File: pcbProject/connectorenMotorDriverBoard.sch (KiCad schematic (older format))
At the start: 16 parts, among them P5 GND, P6 +5V

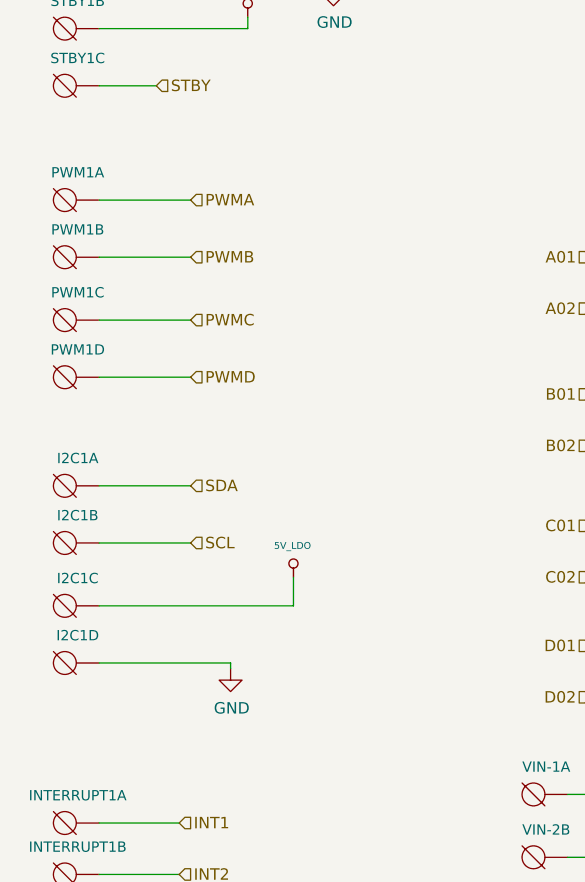
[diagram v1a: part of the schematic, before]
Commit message: TekeningAfenGecontroleerd
nu nog componenten toevoegen en routen
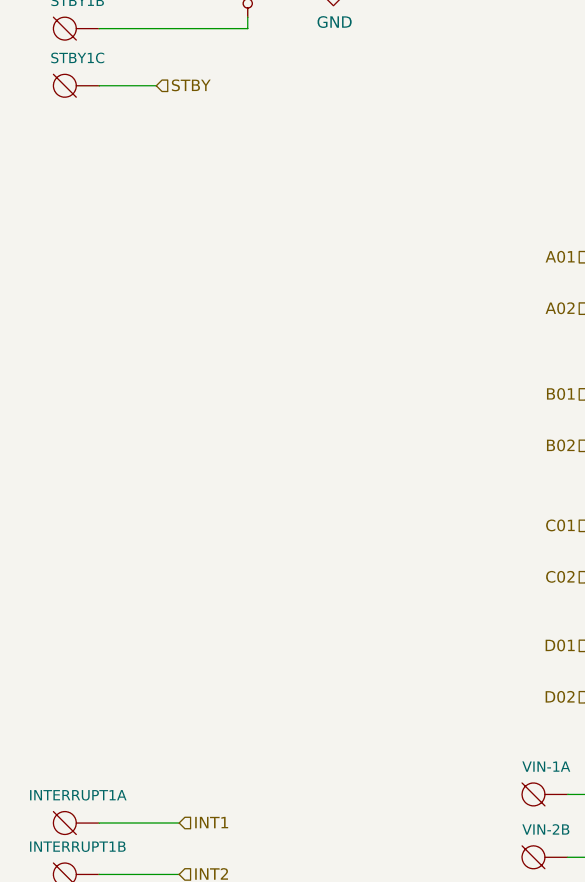
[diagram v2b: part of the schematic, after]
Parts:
- removed I2C1, PWM1: DG3XX-04-3.5, degson_DG350-3.5-04P, symbol degson:DG3XX-04-3.5
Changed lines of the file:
@@
 $Descr A4 11693 8268
 encoding utf-8
-Sheet 11 11
+Sheet 10 11
 Title ""
 Date ""
@@
 Connection ~ 4925 2125
 $Comp
-L degson:DG3XX-04-3.5 PWM1
-U 1 1 5C767F10
-P 1575 2700
-F 0 "PWM1" H 1569 2580 45  0000 C CNN
-F 1 "DG3XX-04-3.5" H 1575 2700 45  0001 L BNN
-F 2 "degson_DG350-3.5-04P" H 1605 2850 20  0001 C CNN
-F 3 "" H 1575 2700 50  0001 C CNN
-	1    1575 2700
-	-1   0    0    1
-$EndComp
-$Comp
-L degson:DG3XX-04-3.5 PWM1
-U 2 1 5C767FA5
-P 1575 2950
-F 0 "PWM1" H 1569 2830 45  0000 C CNN
-F 1 "DG3XX-04-3.5" H 1575 2950 45  0001 L BNN
-F 2 "degson_DG350-3.5-04P" H 1605 3100 20  0001 C CNN
-F 3 "" H 1575 2950 50  0001 C CNN
-	2    1575 2950
-	-1   0    0    1
-$EndComp
-$Comp
-L degson:DG3XX-04-3.5 PWM1
-U 3 1 5C76807E
-P 1575 3225
-F 0 "PWM1" H 1569 3105 45  0000 C CNN
-F 1 "DG3XX-04-3.5" H 1575 3225 45  0001 L BNN
-F 2 "degson_DG350-3.5-04P" H 1605 3375 20  0001 C CNN
-F 3 "" H 1575 3225 50  0001 C CNN
-	3    1575 3225
-	-1   0    0    1
-$EndComp
-$Comp
-L degson:DG3XX-04-3.5 PWM1
-U 4 1 5C768129
-P 1575 3475
-F 0 "PWM1" H 1569 3355 45  0000 C CNN
-F 1 "DG3XX-04-3.5" H 1575 3475 45  0001 L BNN
-F 2 "degson_DG350-3.5-04P" H 1605 3625 20  0001 C CNN
-F 3 "" H 1575 3475 50  0001 C CNN
-	4    1575 3475
-	-1   0    0    1
-$EndComp
-Text HLabel 2075 2700 2    50   Input ~ 0
-PWMA
-Text HLabel 2075 2950 2    50   Input ~ 0
-PWMB
-Text HLabel 2075 3225 2    50   Input ~ 0
-PWMC
-Text HLabel 2075 3475 2    50   Input ~ 0
-PWMD
-Wire Wire Line
-	1675 2700 2075 2700
-Wire Wire Line
-	1675 2950 2075 2950
-Wire Wire Line
-	1675 3225 2075 3225
-Wire Wire Line
-	1675 3475 2075 3475
-$Comp
-L degson:DG3XX-04-3.5 I2C1
-U 1 1 5C769E25
-P 1575 3950
-F 0 "I2C1" H 1569 3830 45  0000 C CNN
-F 1 "DG3XX-04-3.5" H 1575 3950 45  0001 L BNN
-F 2 "degson_DG350-3.5-04P" H 1605 4100 20  0001 C CNN
-F 3 "" H 1575 3950 50  0001 C CNN
-	1    1575 3950
-	-1   0    0    1
-$EndComp
-$Comp
-L degson:DG3XX-04-3.5 I2C1
-U 2 1 5C769E2C
-P 1575 4200
-F 0 "I2C1" H 1569 4080 45  0000 C CNN
-F 1 "DG3XX-04-3.5" H 1575 4200 45  0001 L BNN
-F 2 "degson_DG350-3.5-04P" H 1605 4350 20  0001 C CNN
-F 3 "" H 1575 4200 50  0001 C CNN
-	2    1575 4200
-	-1   0    0    1
-$EndComp
-$Comp
-L degson:DG3XX-04-3.5 I2C1
-U 3 1 5C769E33
-P 1575 4475
-F 0 "I2C1" H 1569 4355 45  0000 C CNN
-F 1 "DG3XX-04-3.5" H 1575 4475 45  0001 L BNN
-F 2 "degson_DG350-3.5-04P" H 1605 4625 20  0001 C CNN
-F 3 "" H 1575 4475 50  0001 C CNN
-	3    1575 4475
-	-1   0    0    1
-$EndComp
-$Comp
-L degson:DG3XX-04-3.5 I2C1
-U 4 1 5C769E3A
-P 1575 4725
-F 0 "I2C1" H 1569 4605 45  0000 C CNN
-F 1 "DG3XX-04-3.5" H 1575 4725 45  0001 L BNN
-F 2 "degson_DG350-3.5-04P" H 1605 4875 20  0001 C CNN
-F 3 "" H 1575 4725 50  0001 C CNN
-	4    1575 4725
-	-1   0    0    1
-$EndComp
-Text HLabel 2075 3950 2    50   Input ~ 0
-SDA
-Text HLabel 2075 4200 2    50   Input ~ 0
-SCL
-Wire Wire Line
-	1675 3950 2075 3950
-Wire Wire Line
-	1675 4200 2075 4200
-$Comp
-L Arduino_Uno_R3_From_Scratch:5V_LDO #PWR0122
-U 1 1 5C76B0F4
-P 2525 4350
-F 0 "#PWR0122" H 2525 4440 20  0001 C CNN
-F 1 "5V_LDO" H 2521 4488 30  0000 C CNN
-F 2 "" H 2525 4350 60  0000 C CNN
-F 3 "" H 2525 4350 60  0000 C CNN
-	1    2525 4350
-	1    0    0    -1
-$EndComp
-Wire Wire Line
-	2525 4475 2525 4350
-Wire Wire Line
-	1675 4475 2525 4475
-$Comp
-L power:GND #PWR0123
-U 1 1 5C76C27D
-P 2250 4750
-F 0 "#PWR0123" H 2250 4500 50  0001 C CNN
-F 1 "GND" H 2255 4577 50  0000 C CNN
-F 2 "" H 2250 4750 50  0001 C CNN
-F 3 "" H 2250 4750 50  0001 C CNN
-	1    2250 4750
-	1    0    0    -1
-$EndComp
-Wire Wire Line
-	2250 4725 2250 4750
-Wire Wire Line
-	1675 4725 2250 4725
-$Comp
 L degson:DG3XX-03-3.5 INTERRUPT1

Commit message: deel1routingpcb
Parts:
- removed INTERRUPT1, STBY1: DG3XX-03-3.5, degson_DG350-3.5-03P, symbol degson:DG3XX-03-3.5
- removed MA-1, MA-2, MB-1, MB-2, MC-1, MC-2, MD-1, MD-2, VIN-1, VIN-2: DG3XX-02-3.5, degson_DG350-3.5-02P, symbol degson:DG3XX-02-3.5
- added GND1: 12V, degson:degson-DG306-5.0-02P, symbol Connector:Conn_01x02_Female
- added J1: INTERRUPT, Connector_PinSocket_2.54mm:PinSocket_1x03_P2.54mm_Vertical, symbol Connector:Conn_01x03_Female
- added J2: STBY, Connector_PinSocket_2.54mm:PinSocket_1x03_P2.54mm_Vertical, symbol Connector:Conn_01x03_Female
- added MA-1A1: MA-2B, degson:degson-DG306-5.0-02P, symbol Connector:Conn_01x02_Female
- added MB-1A1: MB-2B, degson:degson-DG306-5.0-02P, symbol Connector:Conn_01x02_Female
- added MC-1A1: MC-2B, degson:degson-DG306-5.0-02P, symbol Connector:Conn_01x02_Female
- added MD-1A1: MD-2B, degson:degson-DG306-5.0-02P, symbol Connector:Conn_01x02_Female
- P5, P6: footprint (none) -> Connector_PinSocket_2.54mm:PinSocket_1x08_P2.54mm_Vertical
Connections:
- net 5V_LDO: now also J2.2 (Pin_2)
- net A01: now also MA-1A1.1 (Pin_1)
- net A02: now also MA-1A1.2 (Pin_2)
- net B01: now also MB-1A1.1 (Pin_1)
- net B02: now also MB-1A1.2 (Pin_2)
- net C01: now also MC-1A1.1 (Pin_1)
- net C02: now also MC-1A1.2 (Pin_2)
- net D01: now also MD-1A1.1 (Pin_1)
- net D02: now also MD-1A1.2 (Pin_2)
- net GND: now also GND1.1 (Pin_1), J1.1 (Pin_1), J2.1 (Pin_1)
- net INT1: now also J1.2 (Pin_2)
- net INT2: now also J1.3 (Pin_3)
- net STBY: now also J2.3 (Pin_3)
- net VM: now also GND1.2 (Pin_2)

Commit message: verslag
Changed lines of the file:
@@
 	4925 2225 4925 2125
 Connection ~ 4925 2125
-Text HLabel 3825 2950 0    50   Input ~ 0
+Text HLabel 5250 2950 0    50   Input ~ 0
 A01
-Text HLabel 3825 3175 0    50   Input ~ 0
+Text HLabel 5250 3175 0    50   Input ~ 0
 A02
 $Comp
 L power:GND #PWR0125
 U 1 1 5C773A99
-P 4350 5350
-F 0 "#PWR0125" H 4350 5100 50  0001 C CNN
-F 1 "GND" H 4355 5177 50  0000 C CNN
-F 2 "" H 4350 5350 50  0001 C CNN
-F 3 "" H 4350 5350 50  0001 C CNN
-	1    4350 5350
+P 4975 5350
+F 0 "#PWR0125" H 4975 5100 50  0001 C CNN
+F 1 "GND" H 4980 5177 50  0000 C CNN
+F 2 "" H 4975 5350 50  0001 C CNN
+F 3 "" H 4975 5350 50  0001 C CNN
+	1    4975 5350
 	1    0    0    -1
 $EndComp
-Text HLabel 4725 5575 0    50   Input ~ 0
+Text HLabel 5350 5575 0    50   Input ~ 0
 VM
-Text HLabel 3825 4650 0    50   Input ~ 0
+Text HLabel 5250 4650 0    50   Input ~ 0
 D01
-Text HLabel 3825 4875 0    50   Input ~ 0
+Text HLabel 5250 4875 0    50   Input ~ 0
 D02
-Text HLabel 3825 3550 0    50   Input ~ 0
+Text HLabel 5250 3550 0    50   Input ~ 0
 B01
-Text HLabel 3825 3775 0    50   Input ~ 0
+Text HLabel 5250 3775 0    50   Input ~ 0
 B02
-Text HLabel 3825 4125 0    50   Input ~ 0
+Text HLabel 5250 4125 0    50   Input ~ 0
 C01
-Text HLabel 3825 4350 0    50   Input ~ 0
+Text HLabel 5250 4350 0    50   Input ~ 0
 C02
 Wire Wire Line
-	4725 5575 4875 5575
+	5350 5575 5500 5575
 Wire Wire Line
-	4350 5250 4350 5350
+	4975 5250 4975 5350
 $Comp
 L Connector:Conn_01x03_Female J1
@@
 	5550 5250 5550 5275
 Wire Wire Line
-	4350 5250 5550 5250
-Wire Wire Line
-	4875 5575 4875 5375
-Wire Wire Line
-	4875 5375 5550 5375
+	5500 5575 5500 5375
 $Comp
 L Connector:Conn_01x02_Female MD-1A1
@@
 	1    0    0    -1
 $EndComp
-Wire Wire Line
-	3825 2950 5425 2950
-Wire Wire Line
-	4975 3175 4975 3050
-Wire Wire Line
-	4975 3050 5425 3050
-Wire Wire Line
-	3825 3175 4975 3175
-Wire Wire Line
-	3825 3550 5425 3550
-Wire Wire Line
-	5000 3775 5000 3650
-Wire Wire Line
-	5000 3650 5425 3650
-Wire Wire Line
-	3825 3775 5000 3775
-Wire Wire Line
-	3825 4125 5425 4125
-Wire Wire Line
-	4950 4350 4950 4225
-Wire Wire Line
-	4950 4225 5425 4225
-Wire Wire Line
-	3825 4350 4950 4350
-Wire Wire Line
-	3825 4650 5425 4650
-Wire Wire Line
-	5025 4875 5025 4750
-Wire Wire Line
-	5025 4750 5425 4750
-Wire Wire Line
-	3825 4875 5025 4875
 $Comp
 L Connector:Conn_01x03_Female J2
@@
 Wire Wire Line
 	1450 2200 1925 2200
+Wire Wire Line
+	5250 4875 5350 4875
+Wire Wire Line
+	5350 4875 5350 4750
+Wire Wire Line
+	5350 4750 5425 4750
+Wire Wire Line
+	5250 4650 5425 4650
+Wire Wire Line
+	5250 4350 5350 4350
+Wire Wire Line
+	5350 4350 5350 4225
+Wire Wire Line
+	5350 4225 5425 4225
+Wire Wire Line
+	5250 4125 5425 4125
+Wire Wire Line
+	5250 3775 5325 3775
+Wire Wire Line
+	5325 3775 5325 3650
+Wire Wire Line
+	5325 3650 5425 3650
+Wire Wire Line
+	5425 3550 5250 3550
+Wire Wire Line
+	5250 2950 5425 2950
+Wire Wire Line
+	5250 3175 5325 3175
+Wire Wire Line
+	5325 3175 5325 3050
+Wire Wire Line
+	5325 3050 5425 3050
+Wire Wire Line
+	5550 5250 4975 5250
+Wire Wire Line
+	5500 5375 5550 5375
 $EndSCHEMATC
